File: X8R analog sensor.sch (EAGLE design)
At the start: 13 parts, among them IC1 MCP1703CB, U1 ATTINY13SOIC

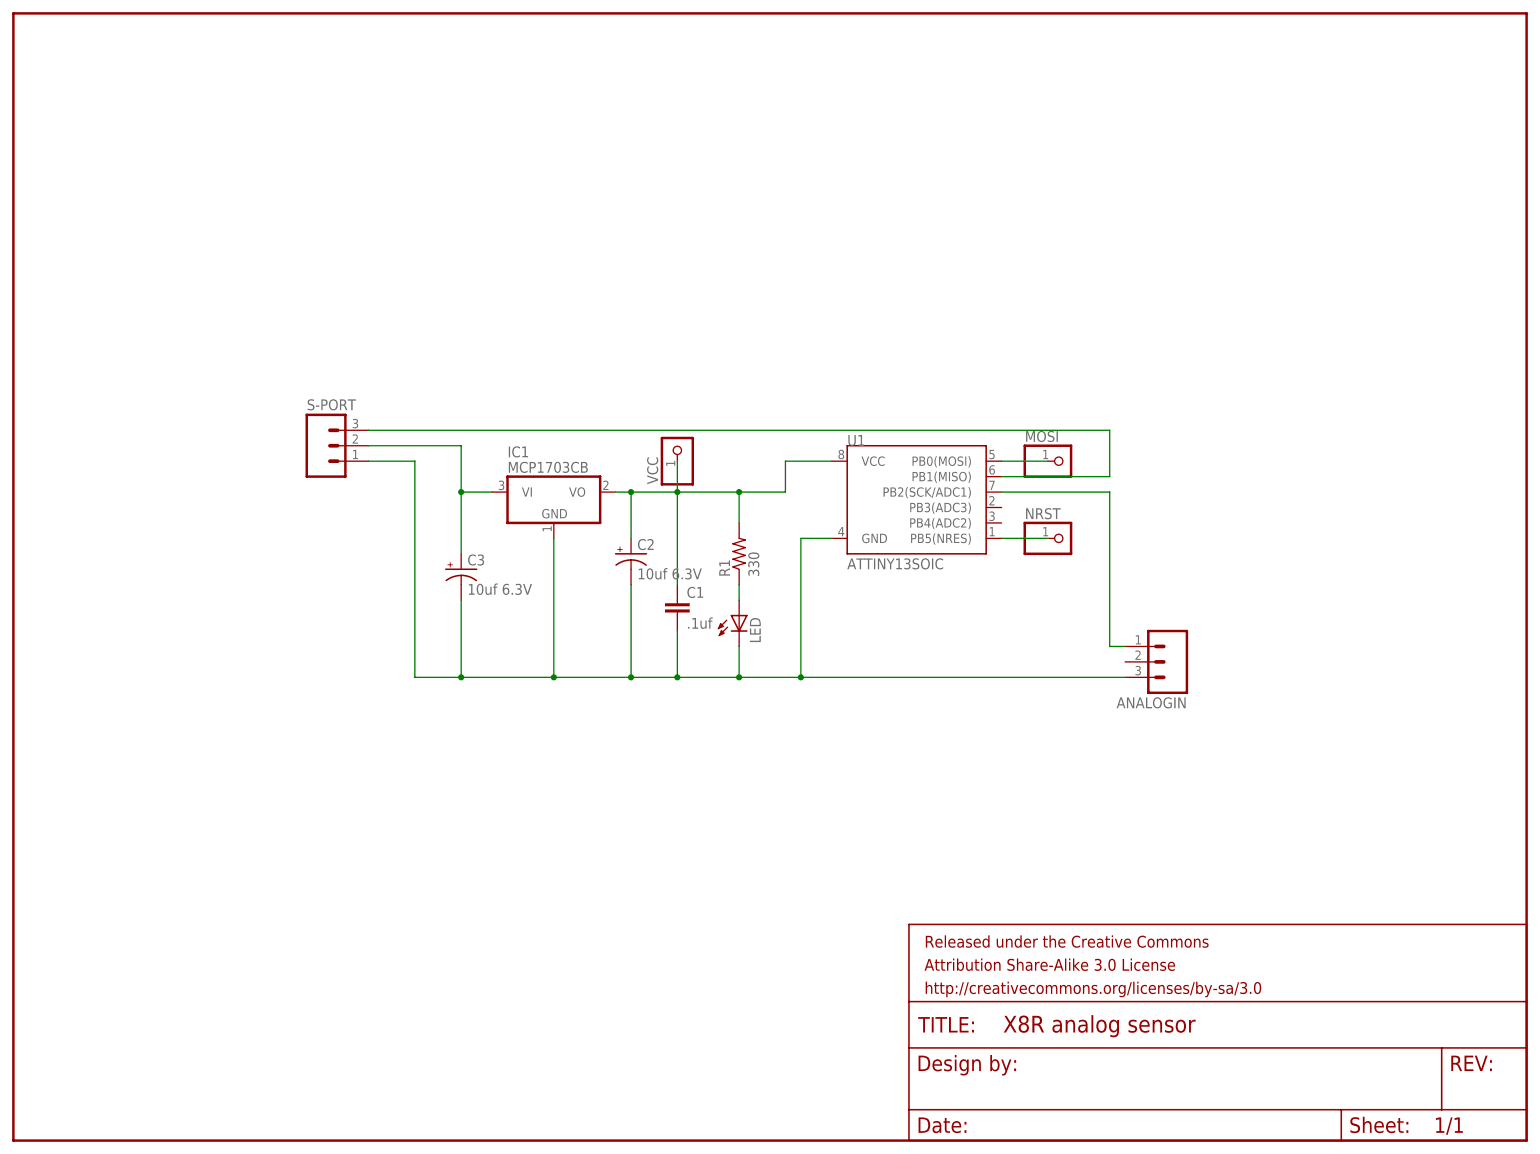
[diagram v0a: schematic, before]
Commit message: updated for voltage divider, and ISP interface
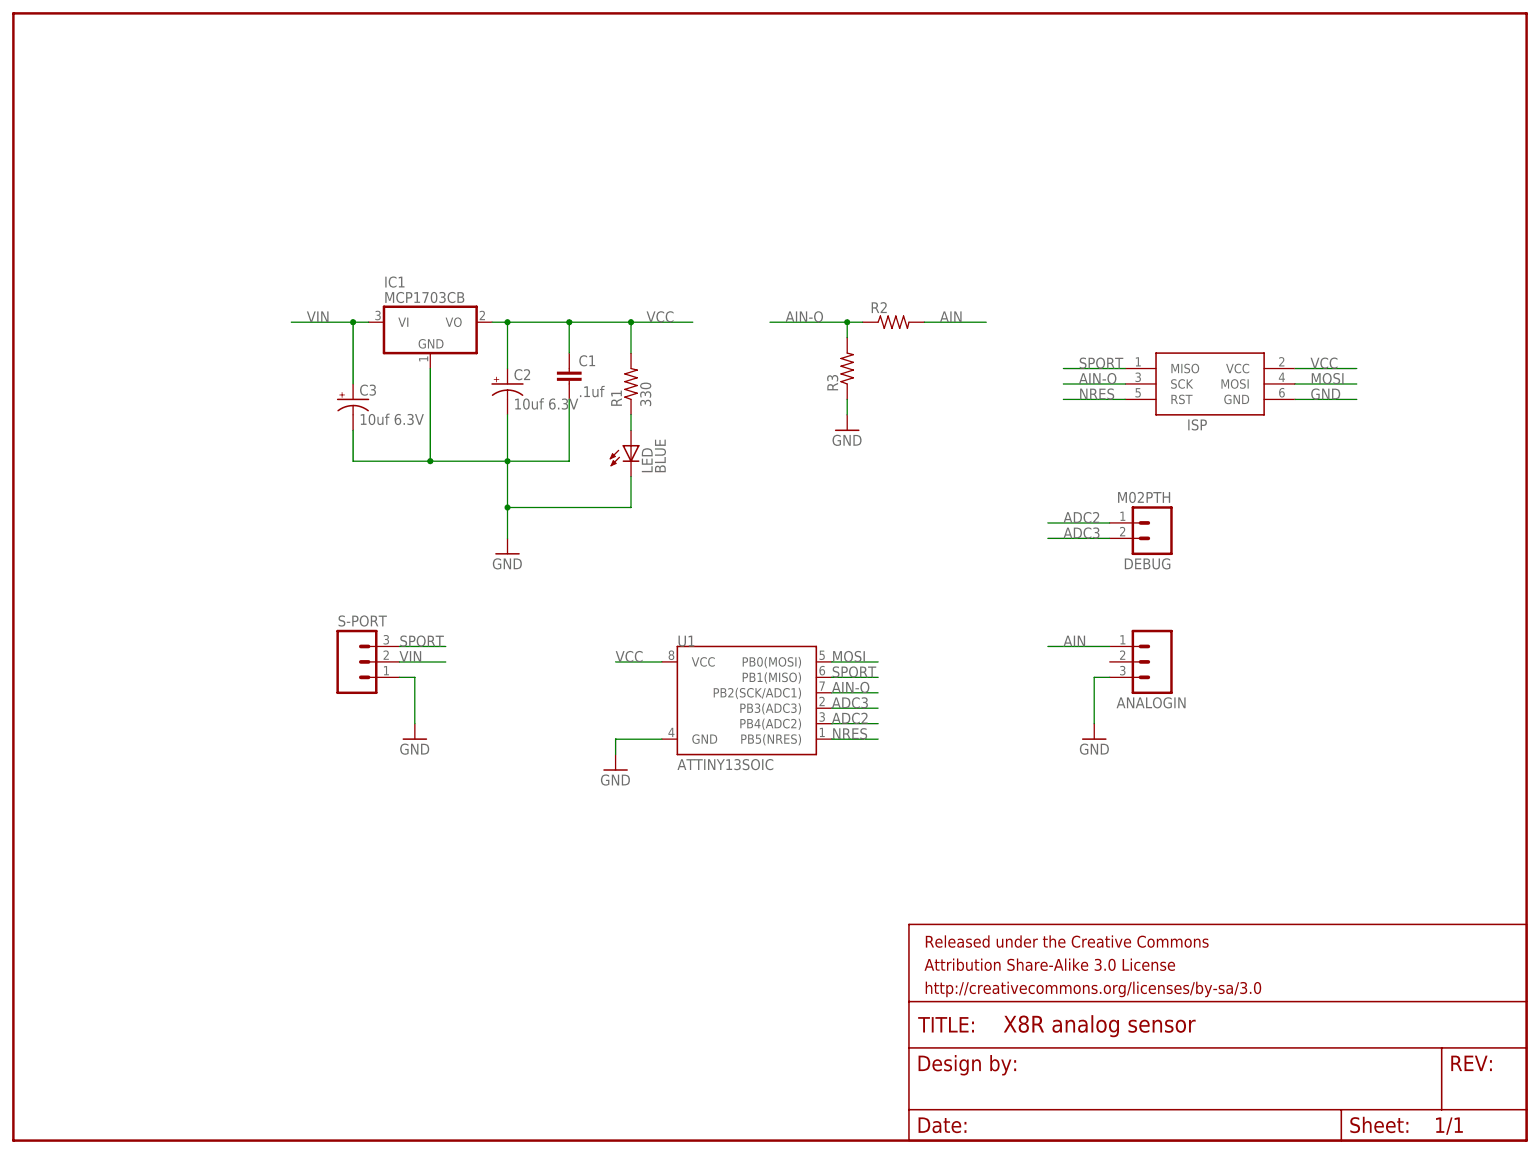
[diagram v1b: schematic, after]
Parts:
- removed MOSI, NRST, VCC: (no value), adafruit:PINHD-1X1CB
- added DEBUG: M02PTH, SparkFun-Connectors:M02PTH
- added ISP: AVRISP-6, adafruit:AVRISP-6
- added R2, R3: (no value), SparkFun-Passives:RESISTORPTH-1/6W
- LED: value (none) -> BLUE
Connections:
- net N$2 renamed VIN
- removed net N$3: S-PORT.3, U1.PB1(MISO)
- removed net N$4: ANALOGIN.1, U1.PB2(SCK/ADC1)
- removed net N$5: MOSI.1, U1.PB0(MOSI)
- removed net N$6: C1.1, C2.+, IC1.VO, R1.2, U1.VCC, VCC.1
- removed net N$8: NRST.1, U1.PB5(NRES)
- new net ADC2: DEBUG.1, U1.PB4(ADC2)
- new net ADC3: DEBUG.2, U1.PB3(ADC3)
- new net AIN: ANALOGIN.1, R2.2
- new net AIN-O: ISP.SCK, R2.1, R3.2, U1.PB2(SCK/ADC1)
- new net MOSI: ISP.MOSI, U1.PB0(MOSI)
- new net NRES: ISP.RST, U1.PB5(NRES)
- new net SPORT: ISP.MISO, S-PORT.3, U1.PB1(MISO)
- new net VCC: C1.1, C2.+, IC1.VO, ISP.VCC, R1.2, U1.VCC
- net GND: now also ISP.GND, R3.1
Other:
- moved on the sheet: ANALOGIN, C1, C2, C3, IC1, LED, R1, S-PORT, U1

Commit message: updated bypass caps as tantalums aren't needed
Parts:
- C2, C3: value 10uf 6.3V -> 1uf; device MyLib:CAP_POL -> SparkFun-Capacitors:CAP0603-CAP
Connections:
- net GND: now also C2.2, C3.2; no longer C2.-, C3.-
- net VCC: now also C3.1; no longer C2.+
- net VIN: now also C2.1; no longer C3.+
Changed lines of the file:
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@@
 <part name="LED" library="SparkFun-LED" deviceset="LED" device="0603" value="BLUE"/>
 <part name="R1" library="SparkFun-Resistors" deviceset="RESISTOR" device="0603" value="330"/>
-<part name="C2" library="MyLib" deviceset="CAP_POL" device="" value="10uf 6.3V"/>
-<part name="C3" library="MyLib" deviceset="CAP_POL" device="" value="10uf 6.3V"/>
 <part name="FRAME1" library="SparkFun-Aesthetics" deviceset="FRAME-LETTER" device=""/>
 <part name="ISP" library="adafruit" deviceset="AVRISP" device="-6"/>
@@
 <part name="R3" library="SparkFun-Passives" deviceset="RESISTOR" device="PTH-1/6W"/>
 <part name="GND5" library="SparkFun-Aesthetics" deviceset="GND" device=""/>
+<part name="C2" library="SparkFun-Capacitors" deviceset="CAP" device="0603-CAP" value="1uf"/>
+<part name="C3" library="SparkFun-Capacitors" deviceset="CAP" device="0603-CAP" value="1uf"/>
+<part name="GND6" library="SparkFun-Aesthetics" deviceset="GND" device=""/>
 </parts>
 <sheets>
@@
 <instance part="LED" gate="G$1" x="101.6" y="114.3"/>
 <instance part="R1" gate="G$1" x="101.6" y="124.46" rot="R90"/>
-<instance part="C2" gate="G$1" x="81.28" y="124.46"/>
-<instance part="C3" gate="G$1" x="55.88" y="121.92"/>
 <instance part="FRAME1" gate="G$1" x="0" y="0"/>
 <instance part="FRAME1" gate="G$2" x="147.32" y="0"/>
@@
 <instance part="R3" gate="G$1" x="137.16" y="127" rot="R90"/>
 <instance part="GND5" gate="1" x="137.16" y="116.84"/>
+<instance part="C2" gate="G$1" x="55.88" y="121.92"/>
+<instance part="C3" gate="G$1" x="81.28" y="121.92"/>
+<instance part="GND6" gate="1" x="73.66" y="106.68"/>
 </instances>
 <busses>
@@
 <net name="GND" class="0">
 <segment>
-<wire x1="55.88" y1="111.76" x2="68.58" y2="111.76" width="0.1524" layer="91"/>
-<wire x1="68.58" y1="111.76" x2="81.28" y2="111.76" width="0.1524" layer="91"/>
-<wire x1="81.28" y1="111.76" x2="91.44" y2="111.76" width="0.1524" layer="91"/>
-<pinref part="IC1" gate="G$1" pin="GND"/>
-<wire x1="68.58" y1="127" x2="68.58" y2="111.76" width="0.1524" layer="91"/>
-<junction x="68.58" y="111.76"/>
-<pinref part="C2" gate="G$1" pin="-"/>
-<wire x1="81.28" y1="119.38" x2="81.28" y2="111.76" width="0.1524" layer="91"/>
-<junction x="81.28" y="111.76"/>
-<pinref part="C3" gate="G$1" pin="-"/>
-<wire x1="55.88" y1="116.84" x2="55.88" y2="111.76" width="0.1524" layer="91"/>
-<pinref part="C1" gate="G$1" pin="2"/>
-<wire x1="91.44" y1="121.92" x2="91.44" y2="111.76" width="0.1524" layer="91"/>
 <pinref part="GND2" gate="1" pin="GND"/>
-<wire x1="81.28" y1="111.76" x2="81.28" y2="104.14" width="0.1524" layer="91"/>
 <pinref part="LED" gate="G$1" pin="C"/>
 <wire x1="81.28" y1="104.14" x2="81.28" y2="99.06" width="0.1524" layer="91"/>
 <wire x1="101.6" y1="109.22" x2="101.6" y2="104.14" width="0.1524" layer="91"/>
 <wire x1="101.6" y1="104.14" x2="81.28" y2="104.14" width="0.1524" layer="91"/>
-<junction x="81.28" y="104.14"/>
 </segment>
 <segment>
@@
 <wire x1="137.16" y1="119.38" x2="137.16" y2="121.92" width="0.1524" layer="91"/>
 </segment>
+<segment>
+<pinref part="IC1" gate="G$1" pin="GND"/>
+<wire x1="68.58" y1="127" x2="68.58" y2="111.76" width="0.1524" layer="91"/>
+<wire x1="55.88" y1="111.76" x2="68.58" y2="111.76" width="0.1524" layer="91"/>
+<pinref part="C2" gate="G$1" pin="2"/>
+<wire x1="55.88" y1="119.38" x2="55.88" y2="111.76" width="0.1524" layer="91"/>
+<pinref part="C3" gate="G$1" pin="2"/>
+<wire x1="81.28" y1="119.38" x2="81.28" y2="111.76" width="0.1524" layer="91"/>
+<pinref part="C1" gate="G$1" pin="2"/>
+<wire x1="91.44" y1="121.92" x2="91.44" y2="111.76" width="0.1524" layer="91"/>
+<wire x1="91.44" y1="111.76" x2="81.28" y2="111.76" width="0.1524" layer="91"/>
+<wire x1="68.58" y1="111.76" x2="73.66" y2="111.76" width="0.1524" layer="91"/>
+<pinref part="GND6" gate="1" pin="GND"/>
+<wire x1="73.66" y1="111.76" x2="81.28" y2="111.76" width="0.1524" layer="91"/>
+<wire x1="73.66" y1="109.22" x2="73.66" y2="111.76" width="0.1524" layer="91"/>
+<junction x="68.58" y="111.76"/>
+<junction x="73.66" y="111.76"/>
+<junction x="81.28" y="111.76"/>
+</segment>
 </net>
 <net name="AIN" class="0">
@@
 <pinref part="IC1" gate="G$1" pin="VO"/>
 <wire x1="78.74" y1="134.62" x2="81.28" y2="134.62" width="0.1524" layer="91"/>
+<pinref part="C1" gate="G$1" pin="1"/>
 <wire x1="81.28" y1="134.62" x2="91.44" y2="134.62" width="0.1524" layer="91"/>
-<pinref part="C1" gate="G$1" pin="1"/>
 <wire x1="91.44" y1="134.62" x2="91.44" y2="129.54" width="0.1524" layer="91"/>
-<pinref part="C2" gate="G$1" pin="+"/>
-<wire x1="81.28" y1="134.62" x2="81.28" y2="127" width="0.1524" layer="91"/>
-<junction x="81.28" y="134.62"/>
 <pinref part="R1" gate="G$1" pin="2"/>
 <wire x1="91.44" y1="134.62" x2="101.6" y2="134.62" width="0.1524" layer="91"/>
@@
 <junction x="101.6" y="134.62"/>
 <label x="104.14" y="134.62" size="1.778" layer="95"/>
+<pinref part="C3" gate="G$1" pin="1"/>
+<wire x1="81.28" y1="127" x2="81.28" y2="134.62" width="0.1524" layer="91"/>
+<junction x="81.28" y="134.62"/>
 </segment>
 <segment>
@@
 <segment>
 <pinref part="IC1" gate="G$1" pin="VI"/>
-<wire x1="55.88" y1="134.62" x2="58.42" y2="134.62" width="0.1524" layer="91"/>
-<pinref part="C3" gate="G$1" pin="+"/>
-<wire x1="55.88" y1="134.62" x2="55.88" y2="124.46" width="0.1524" layer="91"/>
+<wire x1="58.42" y1="134.62" x2="55.88" y2="134.62" width="0.1524" layer="91"/>
+<label x="48.26" y="134.62" size="1.778" layer="95"/>
+<pinref part="C2" gate="G$1" pin="1"/>
+<wire x1="55.88" y1="134.62" x2="45.72" y2="134.62" width="0.1524" layer="91"/>
+<wire x1="55.88" y1="127" x2="55.88" y2="134.62" width="0.1524" layer="91"/>
 <junction x="55.88" y="134.62"/>
-<wire x1="55.88" y1="134.62" x2="45.72" y2="134.62" width="0.1524" layer="91"/>
-<label x="48.26" y="134.62" size="1.778" layer="95"/>
-</segment>
-</net>
+</segment>
+</net>

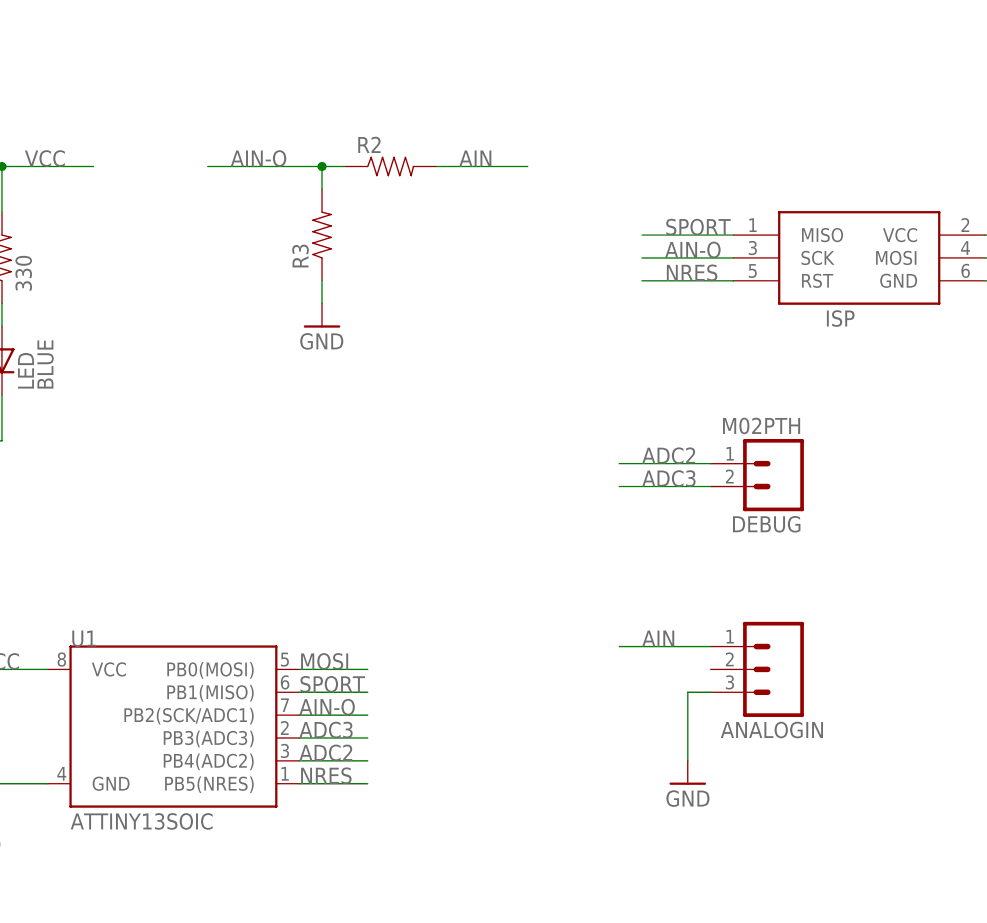
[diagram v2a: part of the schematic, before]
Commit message: updated for a bypass cap on the AIN side, and changed the 3 pin connector for AIN to a 2 pin
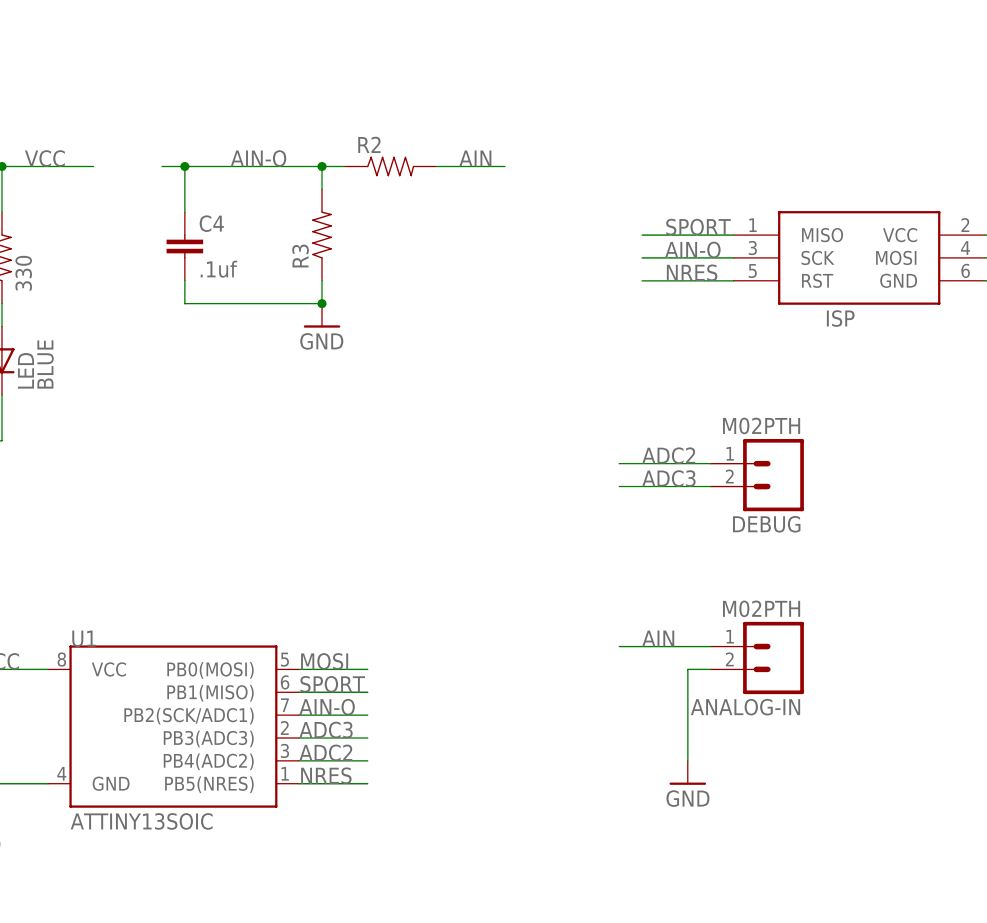
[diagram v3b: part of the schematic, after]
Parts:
- removed ANALOGIN: (no value), SparkFun-Connectors:M03PTH
- added ANALOG-IN: M02PTH, SparkFun-Connectors:M02PTH
- added C4: .1uf, SparkFun-Capacitors:CAP0603-CAP
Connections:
- net AIN: now also ANALOG-IN.1; no longer ANALOGIN.1
- net AIN-O: now also C4.1
- net GND: now also ANALOG-IN.2, C4.2; no longer ANALOGIN.3
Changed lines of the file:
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@@
 <part name="IC1" library="linear" deviceset="MCP1703" device="CB"/>
 <part name="S-PORT" library="SparkFun-Connectors" deviceset="M03" device="PTH"/>
-<part name="ANALOGIN" library="SparkFun-Connectors" deviceset="M03" device="PTH"/>
 <part name="LED" library="SparkFun-LED" deviceset="LED" device="0603" value="BLUE"/>
 <part name="R1" library="SparkFun-Resistors" deviceset="RESISTOR" device="0603" value="330"/>
@@
 <part name="C3" library="SparkFun-Capacitors" deviceset="CAP" device="0603-CAP" value="1uf"/>
 <part name="GND6" library="SparkFun-Aesthetics" deviceset="GND" device=""/>
+<part name="C4" library="SparkFun-Capacitors" deviceset="CAP" device="0603-CAP" value=".1uf"/>
+<part name="ANALOG-IN" library="SparkFun-Connectors" deviceset="M02" device="PTH"/>
 </parts>
 <sheets>
@@
 <instance part="IC1" gate="G$1" x="68.58" y="134.62"/>
 <instance part="S-PORT" gate="G$1" x="55.88" y="78.74"/>
-<instance part="ANALOGIN" gate="G$1" x="187.96" y="78.74" smashed="yes" rot="R180">
-<attribute name="VALUE" x="190.5" y="86.36" size="1.778" layer="96" rot="R180"/>
-<attribute name="NAME" x="193.04" y="72.898" size="1.778" layer="95" rot="R180"/>
-</instance>
 <instance part="LED" gate="G$1" x="101.6" y="114.3"/>
 <instance part="R1" gate="G$1" x="101.6" y="124.46" rot="R90"/>
@@
 <instance part="C3" gate="G$1" x="81.28" y="121.92"/>
 <instance part="GND6" gate="1" x="73.66" y="106.68"/>
+<instance part="C4" gate="G$1" x="121.92" y="124.46"/>
+<instance part="ANALOG-IN" gate="G$1" x="187.96" y="81.28" rot="R180"/>
 </instances>
 <busses>
@@
 </segment>
 <segment>
-<pinref part="ANALOGIN" gate="G$1" pin="3"/>
 <pinref part="GND3" gate="1" pin="GND"/>
-<wire x1="180.34" y1="76.2" x2="177.8" y2="76.2" width="0.1524" layer="91"/>
-<wire x1="177.8" y1="76.2" x2="177.8" y2="68.58" width="0.1524" layer="91"/>
+<wire x1="180.34" y1="78.74" x2="177.8" y2="78.74" width="0.1524" layer="91"/>
+<wire x1="177.8" y1="78.74" x2="177.8" y2="68.58" width="0.1524" layer="91"/>
+<pinref part="ANALOG-IN" gate="G$1" pin="2"/>
 </segment>
 <segment>
@@
 <pinref part="R3" gate="G$1" pin="1"/>
 <wire x1="137.16" y1="119.38" x2="137.16" y2="121.92" width="0.1524" layer="91"/>
+<pinref part="C4" gate="G$1" pin="2"/>
+<wire x1="121.92" y1="121.92" x2="121.92" y2="119.38" width="0.1524" layer="91"/>
+<wire x1="121.92" y1="119.38" x2="137.16" y2="119.38" width="0.1524" layer="91"/>
+<junction x="137.16" y="119.38"/>
 </segment>
 <segment>
@@
 <net name="AIN" class="0">
 <segment>
-<pinref part="ANALOGIN" gate="G$1" pin="1"/>
 <wire x1="170.18" y1="81.28" x2="180.34" y2="81.28" width="0.1524" layer="91"/>
 <label x="172.72" y="81.28" size="1.778" layer="95"/>
+<pinref part="ANALOG-IN" gate="G$1" pin="1"/>
 </segment>
 <segment>
 <pinref part="R2" gate="G$1" pin="2"/>
-<wire x1="149.86" y1="134.62" x2="160.02" y2="134.62" width="0.1524" layer="91"/>
+<wire x1="149.86" y1="134.62" x2="157.48" y2="134.62" width="0.1524" layer="91"/>
 <label x="152.4" y="134.62" size="1.778" layer="95"/>
 </segment>
@@
 <wire x1="137.16" y1="132.08" x2="137.16" y2="134.62" width="0.1524" layer="91"/>
 <wire x1="137.16" y1="134.62" x2="139.7" y2="134.62" width="0.1524" layer="91"/>
-<wire x1="137.16" y1="134.62" x2="124.46" y2="134.62" width="0.1524" layer="91"/>
+<wire x1="137.16" y1="134.62" x2="121.92" y2="134.62" width="0.1524" layer="91"/>
 <label x="127" y="134.62" size="1.778" layer="95"/>
 <junction x="137.16" y="134.62"/>
-</segment>
-</net>
+<pinref part="C4" gate="G$1" pin="1"/>
+<wire x1="121.92" y1="134.62" x2="119.38" y2="134.62" width="0.1524" layer="91"/>
+<wire x1="121.92" y1="129.54" x2="121.92" y2="134.62" width="0.1524" layer="91"/>
+<junction x="121.92" y="134.62"/>
+</segment>
+</net>
